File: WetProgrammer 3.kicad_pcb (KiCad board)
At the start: 2 copper layers, 48 x 25 mm, 40 parts, among them J1 USB_B_Micro, J2 AVR-ISP-6, J3 Conn_01x03_Male, SW1 SW_SPDT, SW2 SW_SPDT, U1 ATmega32U4-AU, U2 TLV1117-33, Y1 16MHz

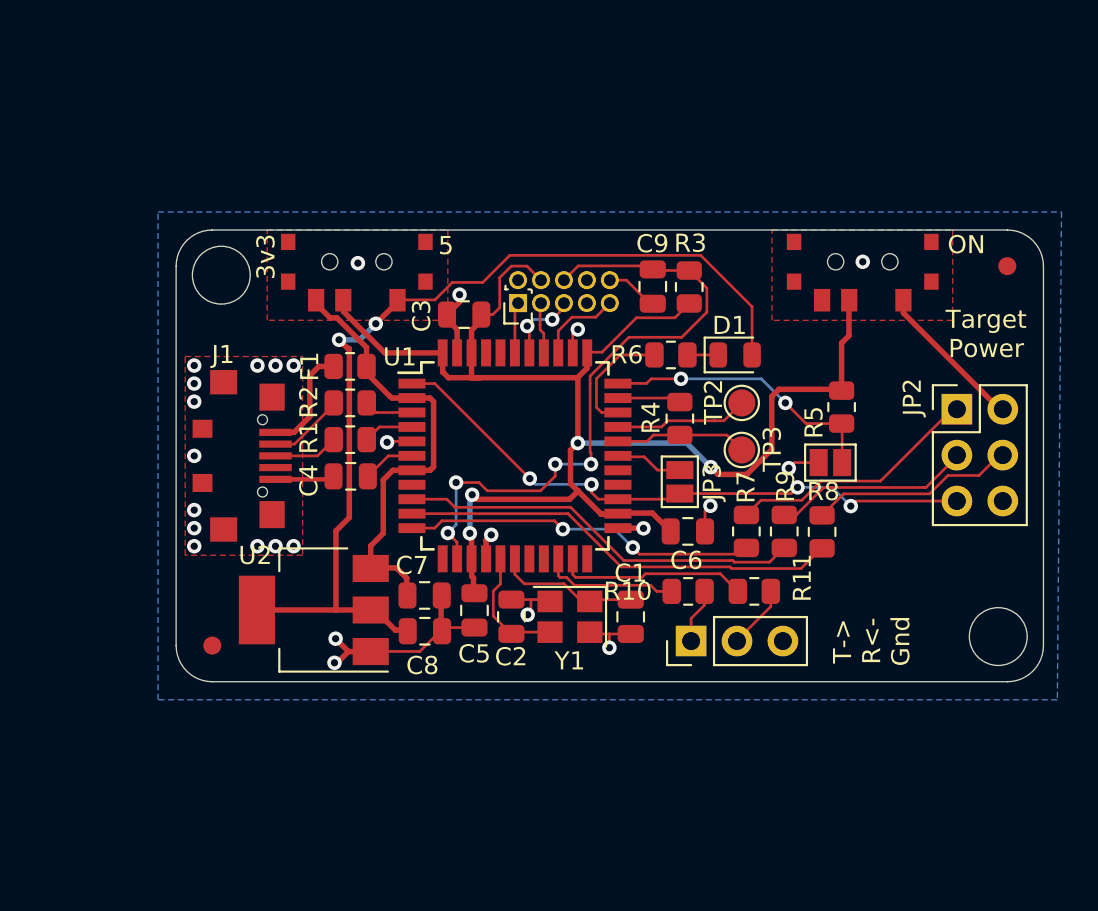
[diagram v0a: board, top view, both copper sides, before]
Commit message: Changed programmer port to JTAG
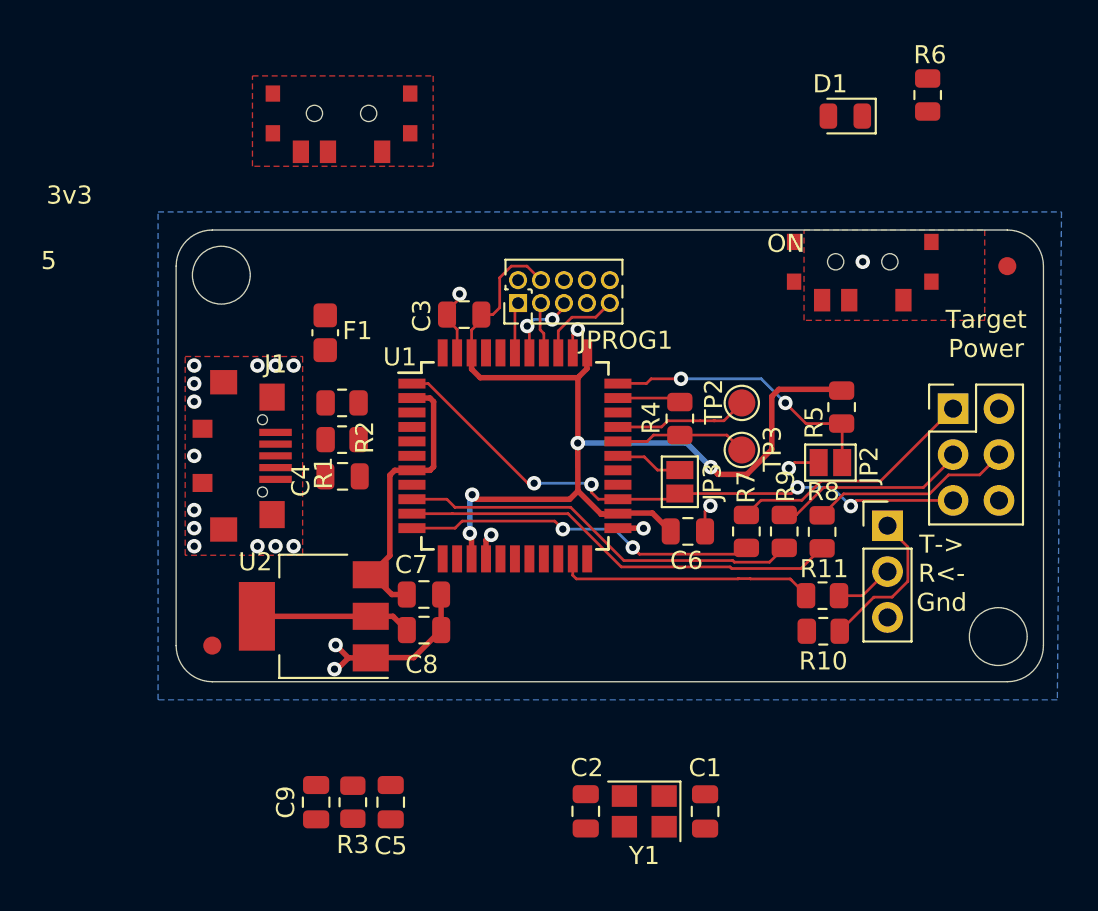
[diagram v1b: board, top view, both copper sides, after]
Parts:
- F1: footprint Resistor_SMD:R_0805_2012Metric -> Fuse:Fuse_0805_2012Metric_Castellated
- moved C9 34.1 mm to (7.75, 6.67)
- moved R3 34.1 mm to (9.78, 6.67)
- moved R6 20.2 mm to (41.6, -32.5), turned to 270 degrees
- moved D1 14.6 mm to (37.0, -31.3), turned to 180 degrees
- moved J3 12.6 mm to (39.4, -8.64), turned to 0 degrees
- moved C5 11.6 mm to (11.9, 6.67)
- moved Y1 11.5 mm to (25.9, 7.18)
- moved C1 11.5 mm to (29.3, 7.18)
- moved C2 11.5 mm to (22.7, 7.17)
- moved wet 10.8 mm to (30.8, -22.9)
- moved SW1 8.26 mm to (9.15, -31.5)
- moved R10 7.80 mm to (35.8, -2.79)
- moved R11 3.78 mm to (35.8, -4.76)
- moved F1 2.32 mm to (8.25, -19.3), turned to 270 degrees
- moved R1 0.45 mm to (9.18, -13.4)
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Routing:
- net +3V3: track 53.0 -> 8.60 mm, vias 2 -> 0
- net /RstP: track 36.1 -> 0.00 mm, vias 4 -> 0
- net VCC: track 82.8 -> 57.9 mm
- net GND: track 36.5 -> 21.2 mm, vias 26 -> 21
- net /VProg: track 8.23 -> 0.00 mm
- net VBUS: track 24.0 -> 15.9 mm
- net /Xtal1: track 7.81 -> 0.00 mm
- net Net-(R10-Pad2): track 7.64 -> 0.00 mm
- net Net-(R6-Pad2): track 6.64 -> 0.00 mm
- net /Xtal2: track 6.58 -> 0.00 mm
- net Net-(F1-Pad2): track 6.41 -> 0.00 mm
- net /TXO: track 3.06 -> 8.46 mm
- net /D-: track 4.18 -> 0.00 mm
- net Net-(R11-Pad2): track 10.6 -> 14.3 mm
- net /D+: track 3.60 -> 0.00 mm
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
